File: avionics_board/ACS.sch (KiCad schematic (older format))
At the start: 26 parts, among them J10 Conn_01x02, J11 Conn_01x02, J9 Conn_01x02, U5 DRV8838, U6 DRV8838, U7 DRV8838

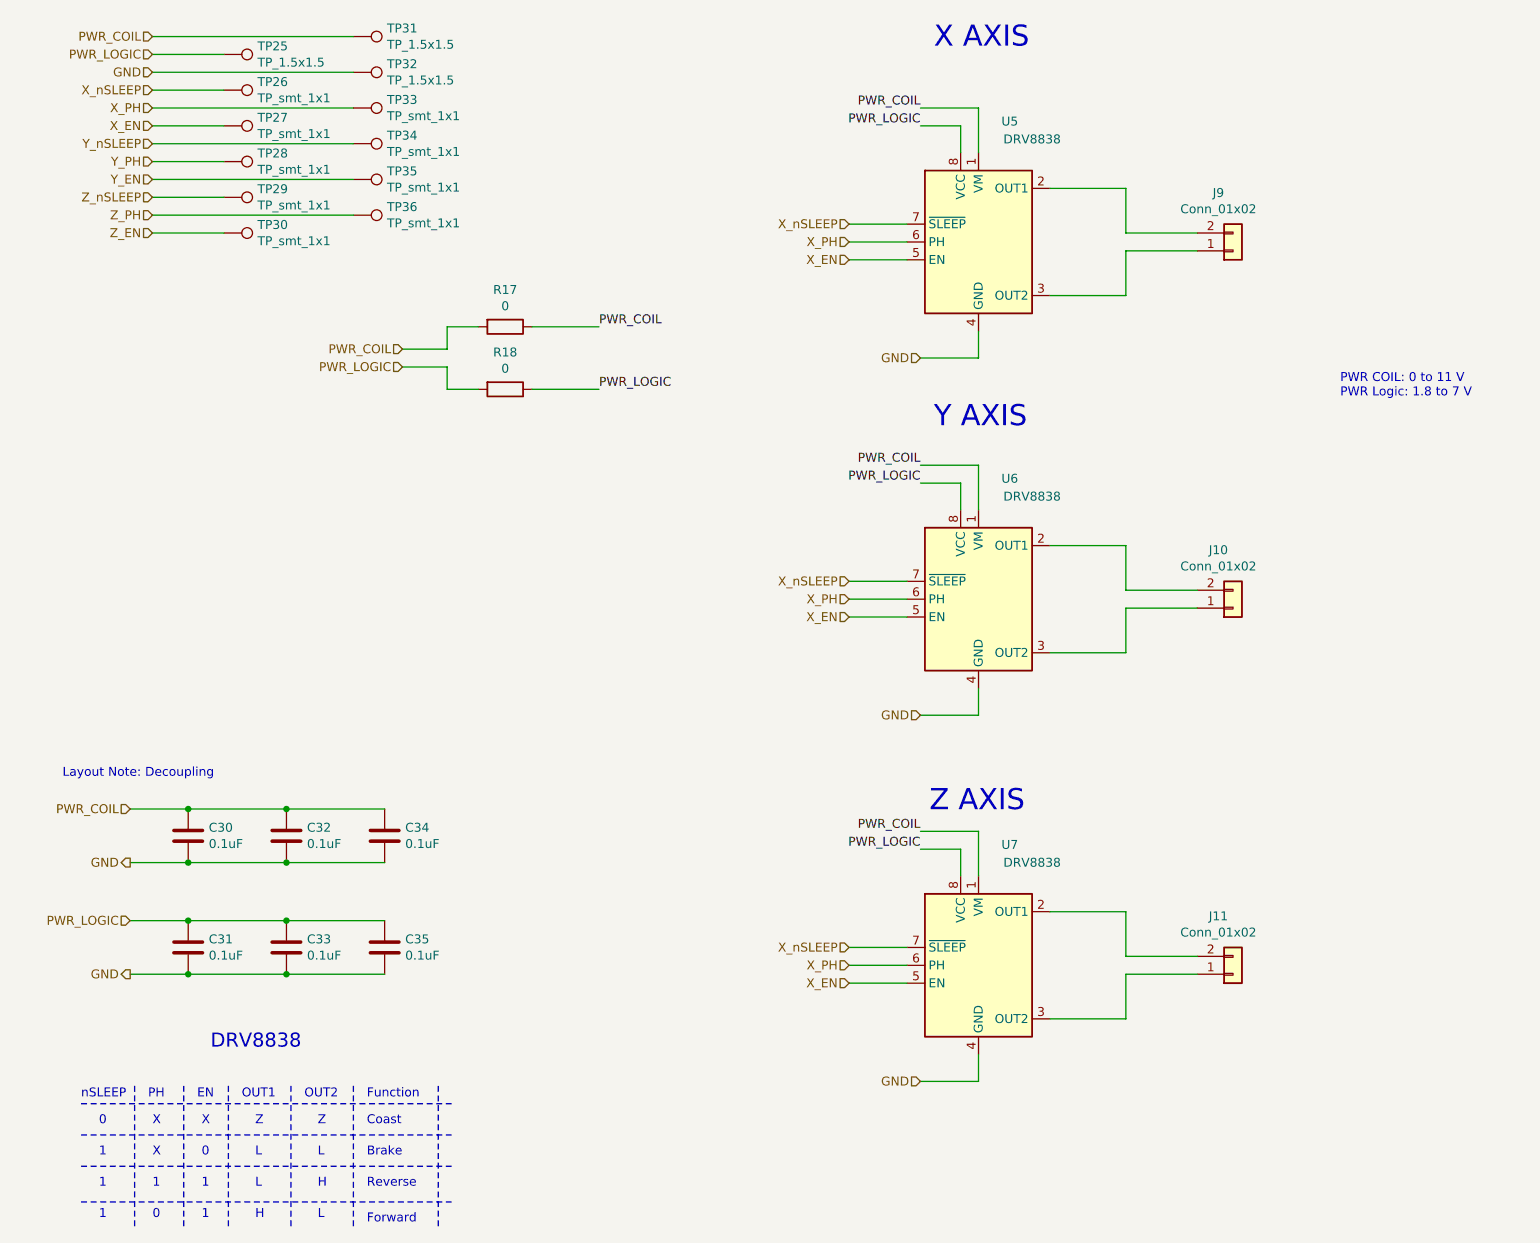
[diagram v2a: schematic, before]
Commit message: Update Avionics part names to match KiCad update. Update Avionics board to use new interboard connector
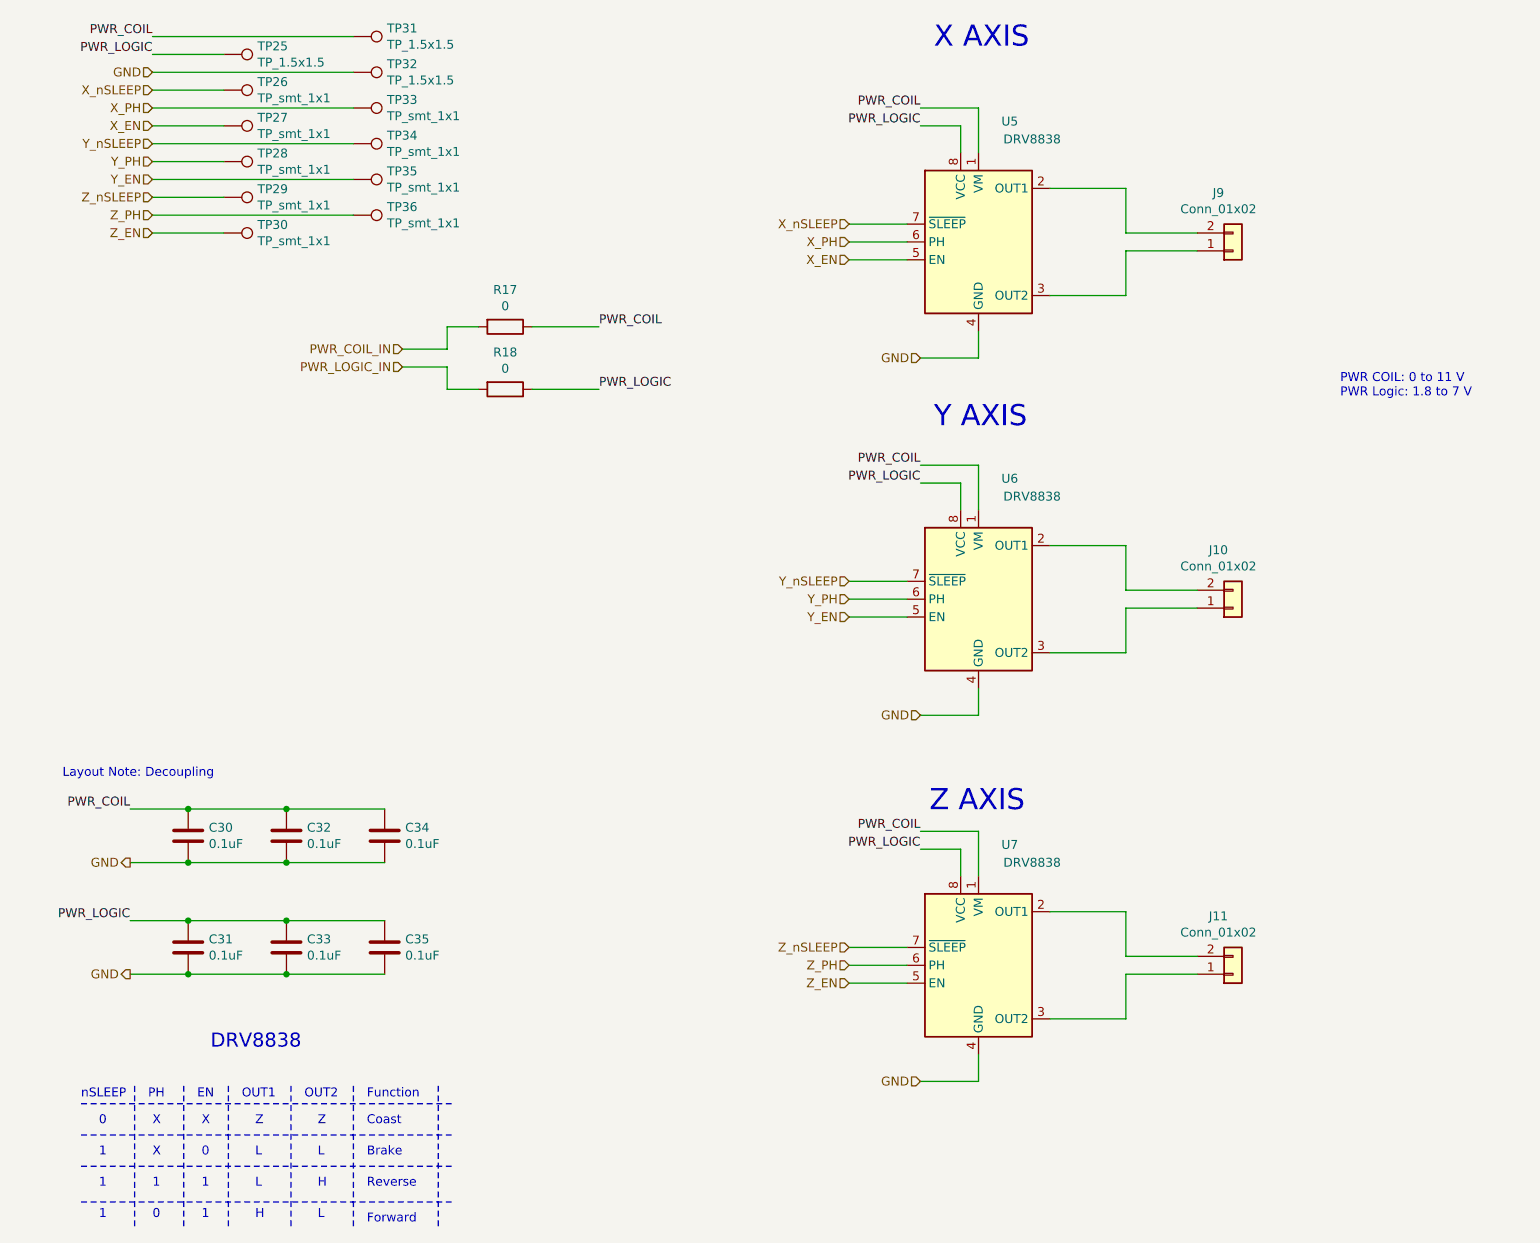
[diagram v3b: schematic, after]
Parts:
- C30, C31, C32, C33, C34, C35: footprint Capacitor_SMD:C_0603_1608Metric_Pad1.05x0.95mm_HandSolder -> Capacitor_SMD:C_0603_1608Metric_Pad1.08x0.95mm_HandSolder
- R17, R18: footprint Resistor_SMD:R_0603_1608Metric_Pad1.05x0.95mm_HandSolder -> Resistor_SMD:R_0603_1608Metric_Pad0.98x0.95mm_HandSolder
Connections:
- net PWR_COIL: no longer R17.2
- net PWR_LOGIC: no longer R18.2
- net X_EN: no longer U6.5 (EN), U7.5 (EN)
- net X_PH: no longer U6.6 (PH), U7.6 (PH)
- net X_nSLEEP: no longer U6.7 (~SLEEP), U7.7 (~SLEEP)
- net Y_EN: now also U6.5 (EN)
- net Y_PH: now also U6.6 (PH)
- net Y_nSLEEP: now also U6.7 (~SLEEP)
- net Z_EN: now also U7.5 (EN)
- net Z_PH: now also U7.6 (PH)
- net Z_nSLEEP: now also U7.7 (~SLEEP)
- new net PWR_COIL_IN: R17.2
- new net PWR_LOGIC_IN: R18.2
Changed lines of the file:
@@
 F 0 "C30" H 1690 5421 50  0000 L CNN
 F 1 "0.1uF" H 1690 5330 50  0000 L CNN
-F 2 "Capacitor_SMD:C_0603_1608Metric_Pad1.05x0.95mm_HandSolder" H 1613 5225 50  0001 C CNN
+F 2 "Capacitor_SMD:C_0603_1608Metric_Pad1.08x0.95mm_HandSolder" H 1613 5225 50  0001 C CNN
 F 3 "~" H 1575 5375 50  0001 C CNN
 F 4 "25V" H 1575 5375 50  0001 C CNN "Voltage"
@@
 Wire Wire Line
 	1575 5225 1250 5225
-Text HLabel 1375 900  0    50   Input ~ 0
-PWR_COIL
-Text HLabel 1375 1000 0    50   Input ~ 0
-PWR_LOGIC
 Text HLabel 1375 1100 0    50   Input ~ 0
 GND
-Text HLabel 1250 5225 0    50   Input ~ 0
-PWR_COIL
-Text HLabel 1250 5850 0    50   Input ~ 0
-PWR_LOGIC
 Text HLabel 1250 6150 0    50   Output ~ 0
 GND
@@
 F 0 "C31" H 1690 6046 50  0000 L CNN
 F 1 "0.1uF" H 1690 5955 50  0000 L CNN
-F 2 "Capacitor_SMD:C_0603_1608Metric_Pad1.05x0.95mm_HandSolder" H 1613 5850 50  0001 C CNN
+F 2 "Capacitor_SMD:C_0603_1608Metric_Pad1.08x0.95mm_HandSolder" H 1613 5850 50  0001 C CNN
 F 3 "~" H 1575 6000 50  0001 C CNN
 F 4 "25V" H 1575 6000 50  0001 C CNN "Voltage"
@@
 Text HLabel 1375 1400 0    50   Input ~ 0
 X_EN
-Text HLabel 1375 1500 0    50   Input ~ 0
-Y_nSLEEP
-Text HLabel 1375 1600 0    50   Input ~ 0
-Y_PH
 Text HLabel 1375 1700 0    50   Input ~ 0
 Y_EN
@@
 $EndComp
 Text HLabel 2775 2650 0    50   Input ~ 0
-PWR_COIL
+PWR_COIL_IN
 Text HLabel 2775 2750 0    50   Input ~ 0
-PWR_LOGIC
+PWR_LOGIC_IN
 Wire Wire Line
 	5675 3400 5900 3400
@@
 Text Notes 5750 3100 0    118  ~ 0
 Y AXIS
-Text HLabel 5275 3950 0    50   Input ~ 0
-X_nSLEEP
-Text HLabel 5275 4050 0    50   Input ~ 0
-X_PH
-Text HLabel 5275 4150 0    50   Input ~ 0
-X_EN
 Wire Wire Line
 	5275 3950 5600 3950
@@
 Text Notes 5725 5250 0    118  ~ 0
 Z AXIS
-Text HLabel 5275 6000 0    50   Input ~ 0
-X_nSLEEP
-Text HLabel 5275 6100 0    50   Input ~ 0
-X_PH
-Text HLabel 5275 6200 0    50   Input ~ 0
-X_EN
 Wire Wire Line
 	5275 6000 5600 6000
@@
 F 0 "C32" H 2240 5421 50  0000 L CNN
 F 1 "0.1uF" H 2240 5330 50  0000 L CNN
-F 2 "Capacitor_SMD:C_0603_1608Metric_Pad1.05x0.95mm_HandSolder" H 2163 5225 50  0001 C CNN
+F 2 "Capacitor_SMD:C_0603_1608Metric_Pad1.08x0.95mm_HandSolder" H 2163 5225 50  0001 C CNN
 F 3 "~" H 2125 5375 50  0001 C CNN
 F 4 "25V" H 2125 5375 50  0001 C CNN "Voltage"
@@
 F 0 "C34" H 2790 5421 50  0000 L CNN
 F 1 "0.1uF" H 2790 5330 50  0000 L CNN
-F 2 "Capacitor_SMD:C_0603_1608Metric_Pad1.05x0.95mm_HandSolder" H 2713 5225 50  0001 C CNN
+F 2 "Capacitor_SMD:C_0603_1608Metric_Pad1.08x0.95mm_HandSolder" H 2713 5225 50  0001 C CNN
 F 3 "~" H 2675 5375 50  0001 C CNN
 F 4 "25V" H 2675 5375 50  0001 C CNN "Voltage"
@@
 F 0 "C33" H 2240 6046 50  0000 L CNN
 F 1 "0.1uF" H 2240 5955 50  0000 L CNN
-F 2 "Capacitor_SMD:C_0603_1608Metric_Pad1.05x0.95mm_HandSolder" H 2163 5850 50  0001 C CNN
+F 2 "Capacitor_SMD:C_0603_1608Metric_Pad1.08x0.95mm_HandSolder" H 2163 5850 50  0001 C CNN
 F 3 "~" H 2125 6000 50  0001 C CNN
 F 4 "25V" H 2125 6000 50  0001 C CNN "Voltage"
@@
 F 0 "C35" H 2790 6046 50  0000 L CNN
 F 1 "0.1uF" H 2790 5955 50  0000 L CNN
-F 2 "Capacitor_SMD:C_0603_1608Metric_Pad1.05x0.95mm_HandSolder" H 2713 5850 50  0001 C CNN
+F 2 "Capacitor_SMD:C_0603_1608Metric_Pad1.08x0.95mm_HandSolder" H 2713 5850 50  0001 C CNN
 F 3 "~" H 2675 6000 50  0001 C CNN
 F 4 "25V" H 2675 6000 50  0001 C CNN "Voltage"
@@
 F 0 "R17" V 3143 2525 50  0000 C CNN
 F 1 "0" V 3234 2525 50  0000 C CNN
-F 2 "Resistor_SMD:R_0603_1608Metric_Pad1.05x0.95mm_HandSolder" V 3280 2525 50  0001 C CNN
+F 2 "Resistor_SMD:R_0603_1608Metric_Pad0.98x0.95mm_HandSolder" V 3280 2525 50  0001 C CNN
 F 3 "~" H 3350 2525 50  0001 C CNN
 F 4 "RK73Z1JTTD" H 3350 2525 50  0001 C CNN "Mfr. #"
@@
 F 0 "R18" V 3143 2875 50  0000 C CNN
 F 1 "0" V 3234 2875 50  0000 C CNN
-F 2 "Resistor_SMD:R_0603_1608Metric_Pad1.05x0.95mm_HandSolder" V 3280 2875 50  0001 C CNN
+F 2 "Resistor_SMD:R_0603_1608Metric_Pad0.98x0.95mm_HandSolder" V 3280 2875 50  0001 C CNN
 F 3 "~" H 3350 2875 50  0001 C CNN
 F 4 "RK73Z1JTTD" H 3350 2875 50  0001 C CNN "Mfr. #"
@@
 Text Notes 8025 2925 0    50   ~ 0
 PWR COIL: 0 to 11 V\nPWR Logic: 1.8 to 7 V
+Text HLabel 1375 1600 0    50   Input ~ 0
+Y_PH
+Text HLabel 1375 1500 0    50   Input ~ 0
+Y_nSLEEP
+Text HLabel 5275 4150 0    50   Input ~ 0
+Y_EN
+Text HLabel 5275 4050 0    50   Input ~ 0
+Y_PH
+Text HLabel 5275 3950 0    50   Input ~ 0
+Y_nSLEEP
+Text HLabel 5275 6000 0    50   Input ~ 0
+Z_nSLEEP
+Text HLabel 5275 6100 0    50   Input ~ 0
+Z_PH
+Text HLabel 5275 6200 0    50   Input ~ 0
+Z_EN
+Text Label 1250 5225 2    50   ~ 0
+PWR_COIL
+Text Label 1250 5850 2    50   ~ 0
+PWR_LOGIC
+Text Label 1375 1000 2    50   ~ 0
+PWR_LOGIC
+Text Label 1375 900  2    50   ~ 0
+PWR_COIL
 $EndSCHEMATC

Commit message: Avionics Board layout done
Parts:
- removed TP25: TP_1.5x1.5, TestPoint:TestPoint_THTPad_1.5x1.5mm_Drill0.7mm, symbol 1K_Custom_Symbol:TP_1.5x1.5
- J10, J11, J9: footprint Connector_PinHeader_1.27mm:PinHeader_1x02_P1.27mm_Vertical -> Connector_PinHeader_2.54mm:PinHeader_1x02_P2.54mm_Vertical
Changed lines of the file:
@@
 F 0 "J9" H 7343 1775 50  0000 C CNN
 F 1 "Conn_01x02" H 7343 1866 50  0000 C CNN
-F 2 "Connector_PinHeader_1.27mm:PinHeader_1x02_P1.27mm_Vertical" H 7425 2100 50  0001 C CNN
+F 2 "Connector_PinHeader_2.54mm:PinHeader_1x02_P2.54mm_Vertical" H 7425 2100 50  0001 C CNN
 F 3 "~" H 7425 2100 50  0001 C CNN
 	1    7425 2100
@@
 F 0 "J10" H 7343 3775 50  0000 C CNN
 F 1 "Conn_01x02" H 7343 3866 50  0000 C CNN
-F 2 "Connector_PinHeader_1.27mm:PinHeader_1x02_P1.27mm_Vertical" H 7425 4100 50  0001 C CNN
+F 2 "Connector_PinHeader_2.54mm:PinHeader_1x02_P2.54mm_Vertical" H 7425 4100 50  0001 C CNN
 F 3 "~" H 7425 4100 50  0001 C CNN
 	1    7425 4100
@@
 F 0 "J11" H 7343 5825 50  0000 C CNN
 F 1 "Conn_01x02" H 7343 5916 50  0000 C CNN
-F 2 "Connector_PinHeader_1.27mm:PinHeader_1x02_P1.27mm_Vertical" H 7425 6150 50  0001 C CNN
+F 2 "Connector_PinHeader_2.54mm:PinHeader_1x02_P2.54mm_Vertical" H 7425 6150 50  0001 C CNN
 F 3 "~" H 7425 6150 50  0001 C CNN
 	1    7425 6150
@@
 $EndComp
 $Comp
-L 1K_Custom_Symbol:TP_1.5x1.5 TP25
-U 1 1 5EC3BC0C
-P 1775 1000
-F 0 "TP25" V 1729 1188 50  0000 L CNN
-F 1 "TP_1.5x1.5" V 1820 1188 50  0000 L CNN
-F 2 "TestPoint:TestPoint_THTPad_1.5x1.5mm_Drill0.7mm" H 1975 1000 50  0001 C CNN
-F 3 "~" H 1975 1000 50  0001 C CNN
-	1    1775 1000
-	0    1    1    0
-$EndComp
-$Comp
 L 1K_Custom_Symbol:TP_1.5x1.5 TP32
 U 1 1 5EC3F304
@@
 Wire Wire Line
 	1375 900  2500 900
-Wire Wire Line
-	1775 1000 1375 1000
 Wire Wire Line
 	1375 1100 2500 1100
@@
 Text Label 1250 5850 2    50   ~ 0
 PWR_LOGIC
-Text Label 1375 1000 2    50   ~ 0
-PWR_LOGIC
 Text Label 1375 900  2    50   ~ 0
